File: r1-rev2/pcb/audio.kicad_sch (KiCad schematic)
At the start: 22 parts, among them J4 HP_3.5mm, J5 LO_3.5mm, Q2 AO3401A, Q3 AO3401A, U6 TLV320AIC3104

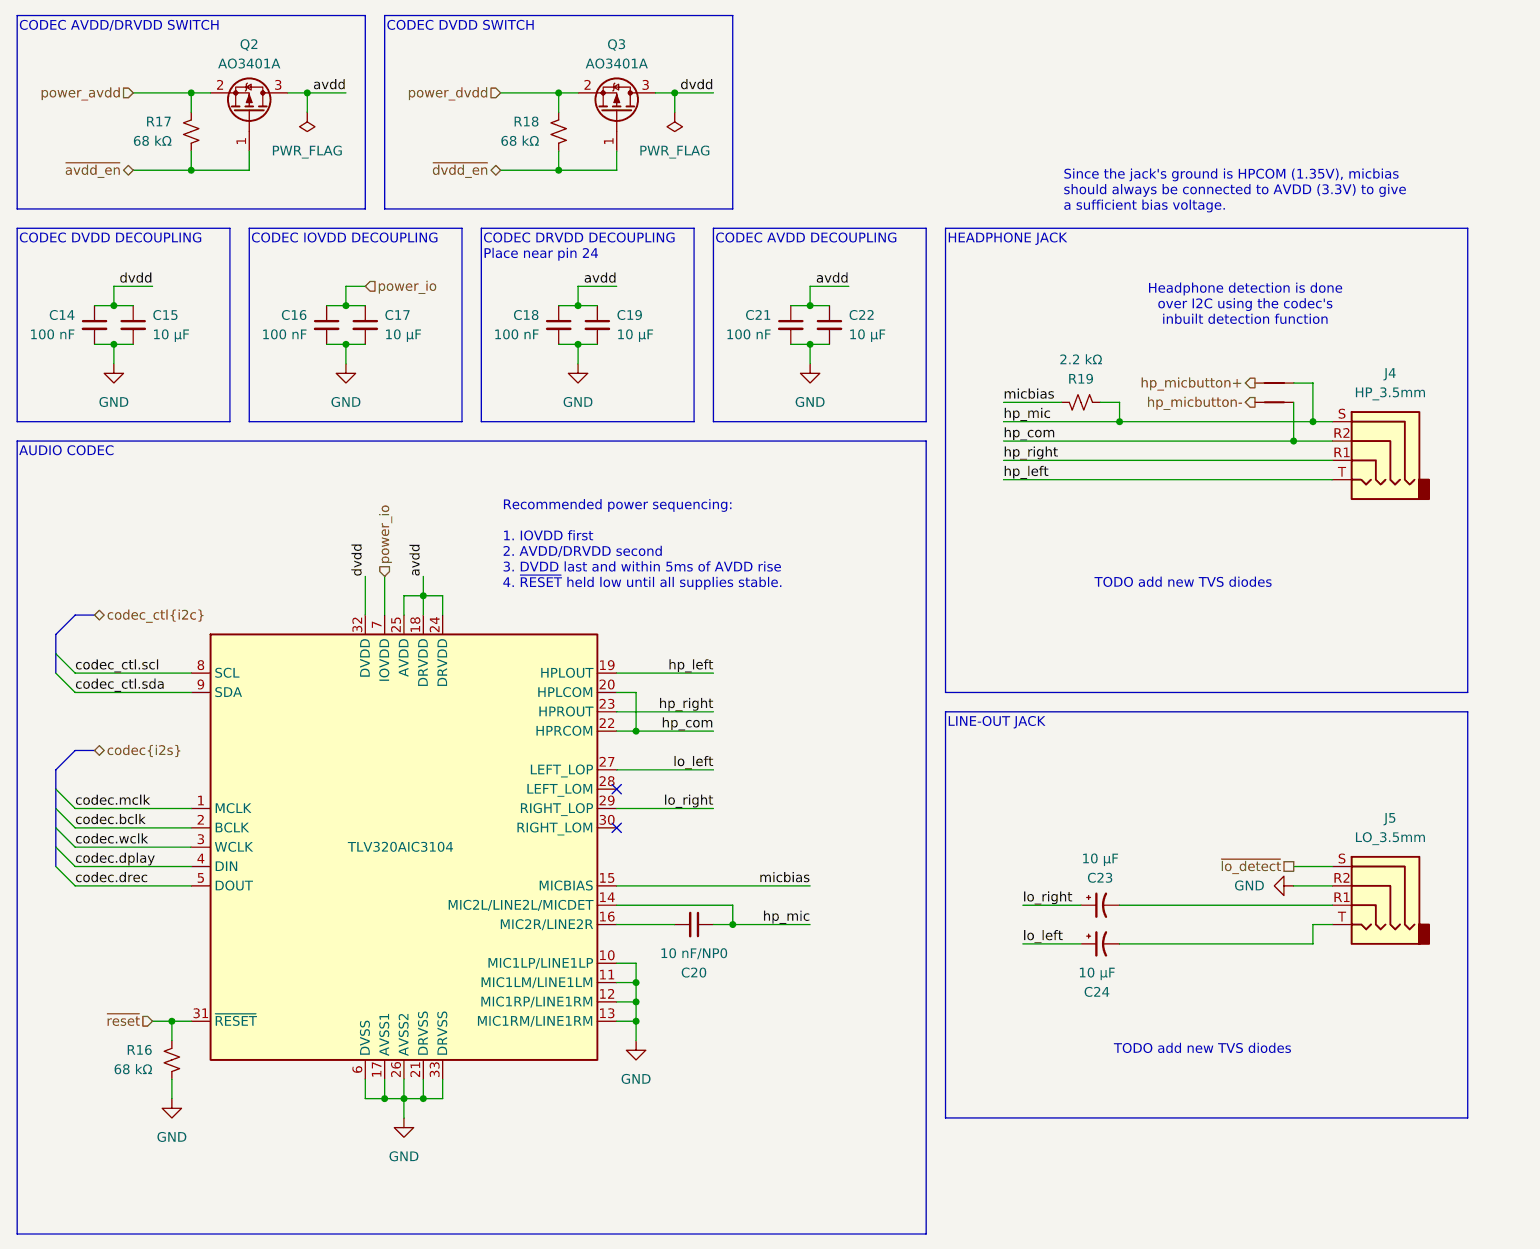
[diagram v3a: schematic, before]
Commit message: R1-Rev2: add TVS diodes to external connectors
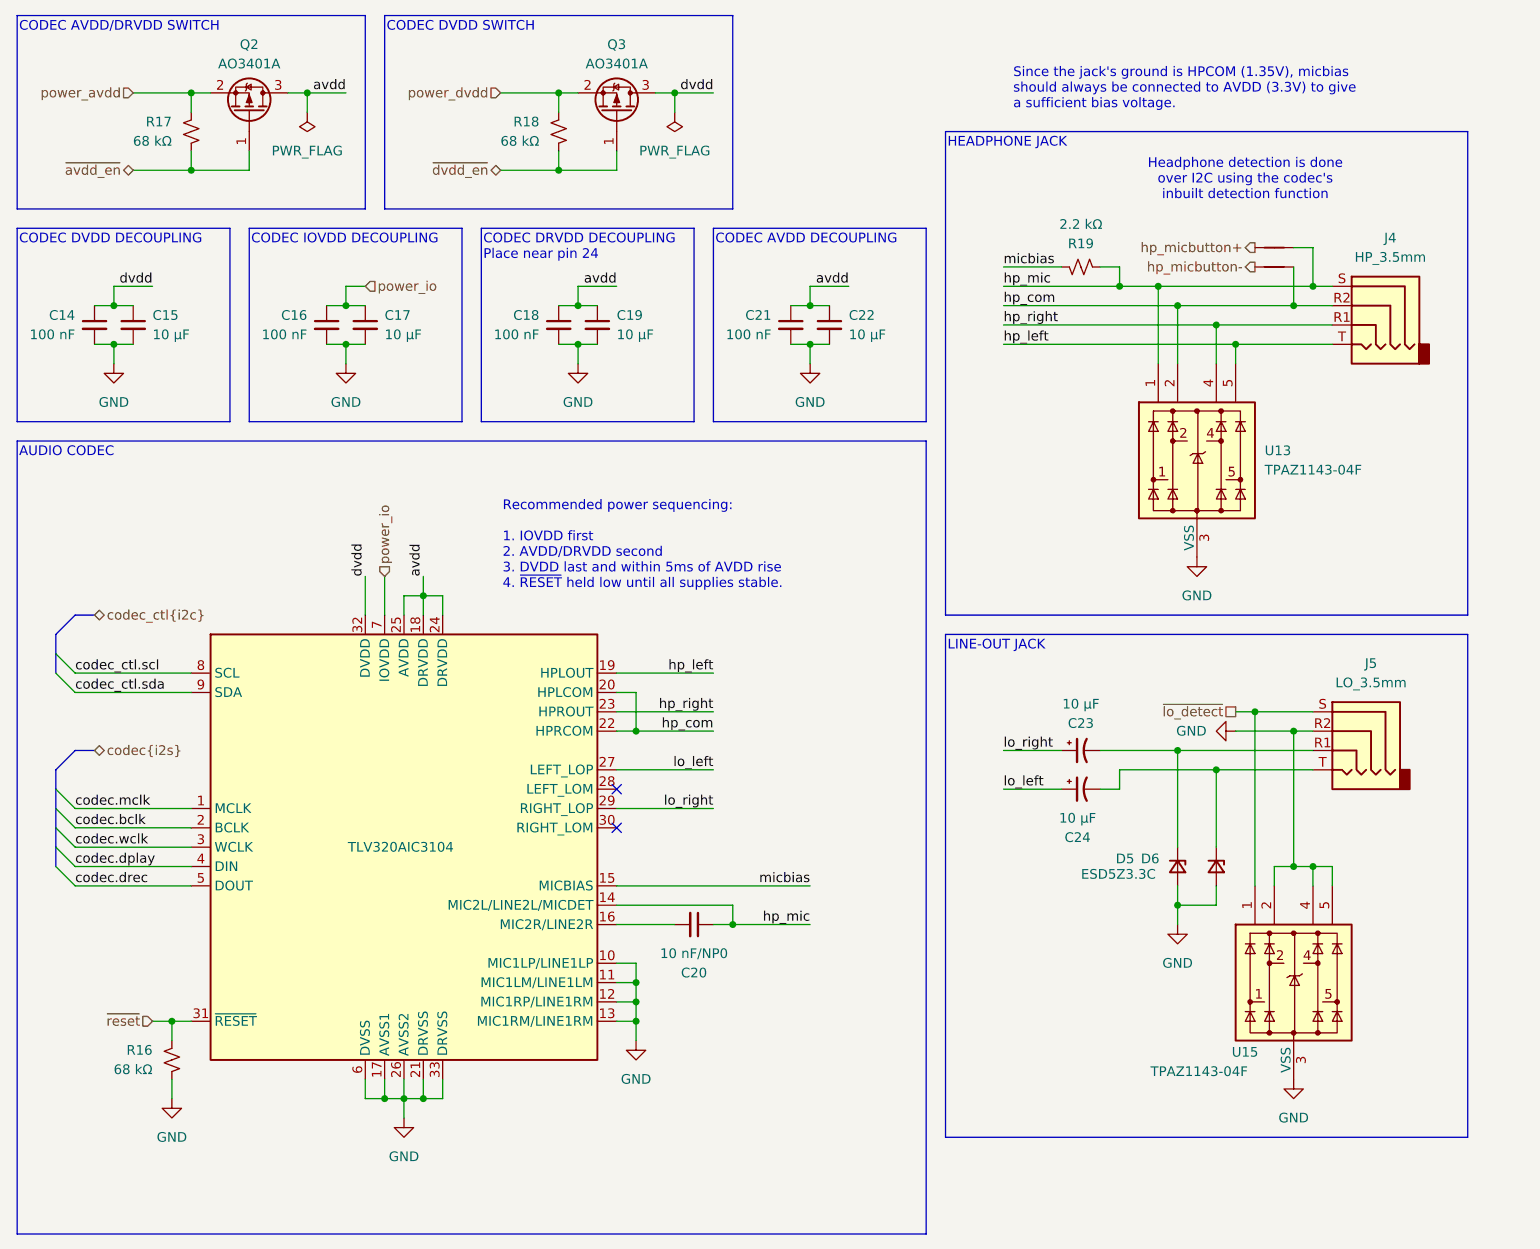
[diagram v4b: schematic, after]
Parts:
- added D5, D6: ESD5Z3.3C, Diode_SMD:D_SOD-523, symbol Device:D_Zener_Small
- added U13, U15: TPAZ1143-04F, echoplayer:TECHPUBLIC_UDFN-10_1.0x2.5mm_P0.5mm, symbol echoplayer:TPAZ1143-04F
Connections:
- net GND: now also D5.2 (A), D6.2 (A), U13.10 (NC), U13.3 (VSS), U13.6 (NC), U13.7 (NC), U13.8 (VSS), U13.9 (NC), U15.10 (NC), U15.2, U15.3 (VSS), U15.4, U15.5, U15.6 (NC), U15.7 (NC), U15.8 (VSS), U15.9 (NC)
- net hp_com: now also U13.2
- net hp_left: now also U13.5
- net hp_mic: now also U13.1
- net hp_right: now also U13.4
- net ~{lo_detect}: now also U15.1
- net at C23.2, J5.R1: now also D5.1 (K)
- net at C24.2, J5.T: now also D6.1 (K)
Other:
- note removed: "TODO add new TVS diodes"
- moved on the sheet: C23, C24, J4, J5, R19

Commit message: R1-Rev2: updates to PCB layout, add HyperRAM routing
- Reannotate schematic and assign footprints for passives
- First try at HyperRAM routing
- Fixed incorrect W958D8NBYA5I pinout
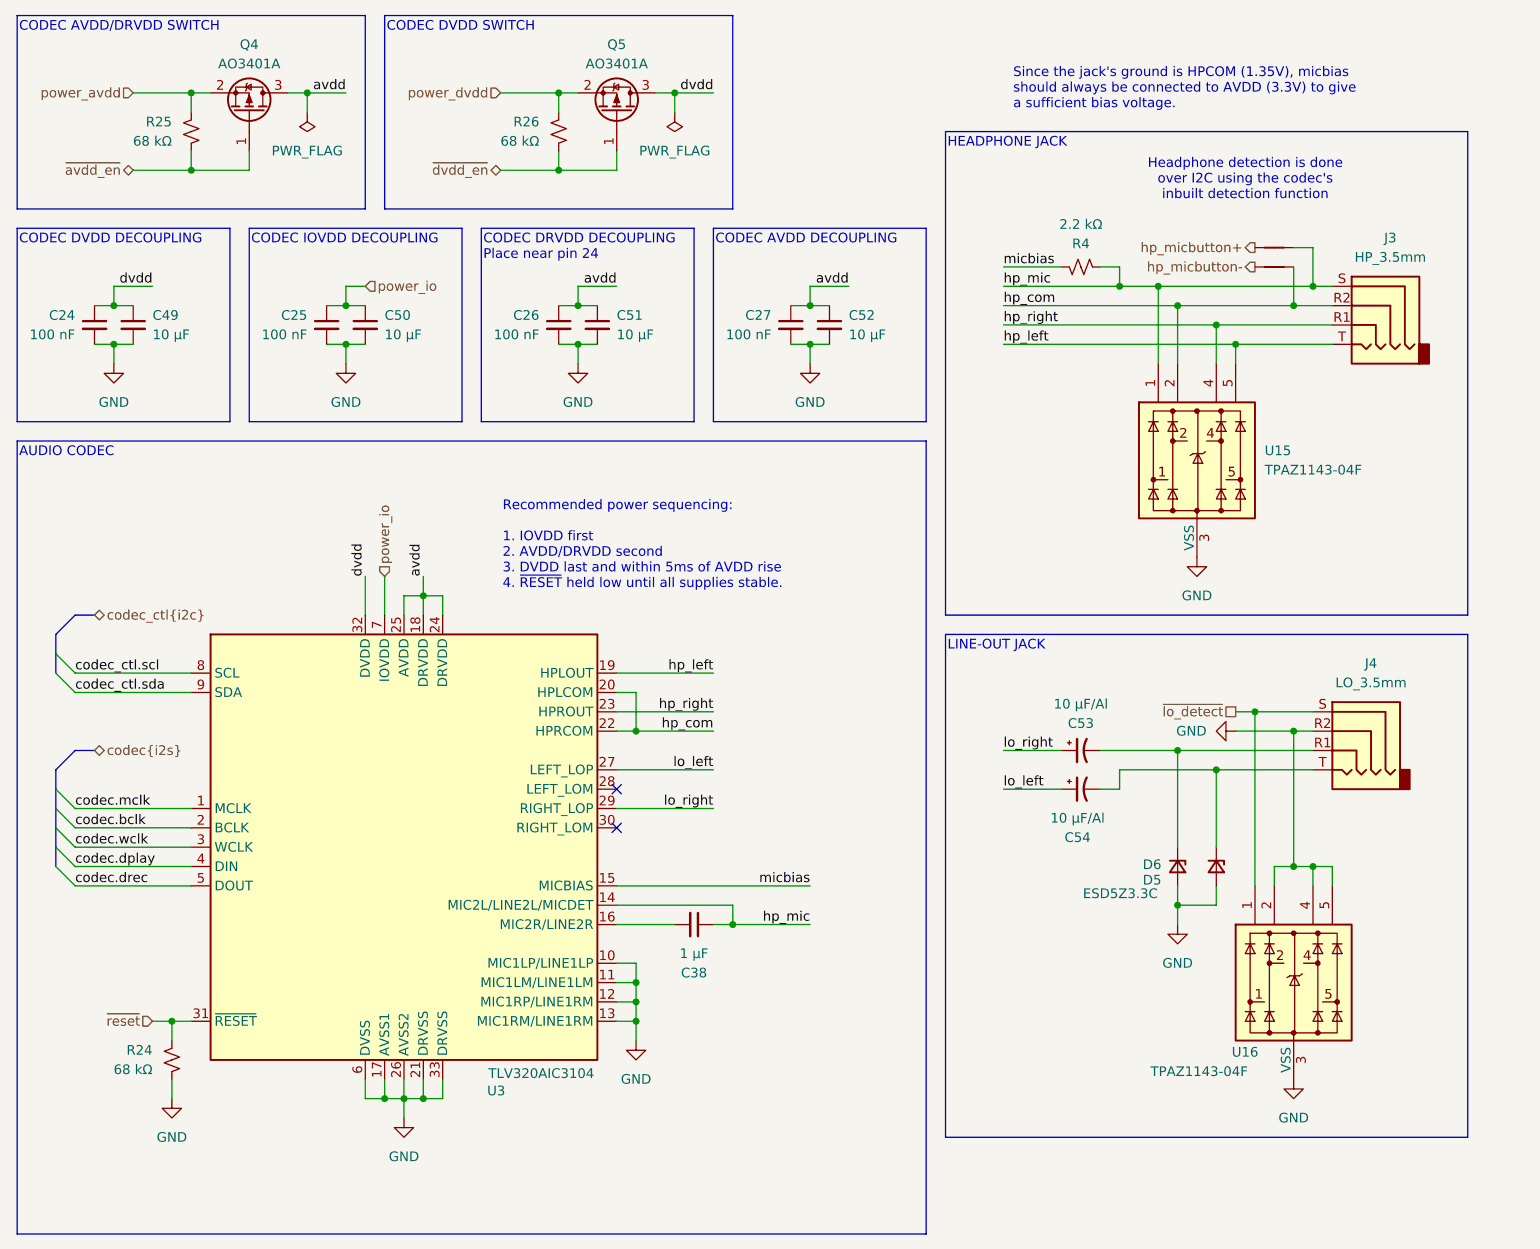
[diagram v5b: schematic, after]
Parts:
- C38: renamed from C20; value 10 nF/NP0 -> 1 µF; footprint Capacitor_SMD:C_0603_1608Metric -> Capacitor_SMD:C_0402_1005Metric
- C49: renamed from C15; footprint Capacitor_SMD:C_0603_1608Metric -> Capacitor_SMD:C_0805_2012Metric
- C50: renamed from C17; footprint Capacitor_SMD:C_0603_1608Metric -> Capacitor_SMD:C_0805_2012Metric
- C51: renamed from C19; footprint Capacitor_SMD:C_0603_1608Metric -> Capacitor_SMD:C_0805_2012Metric
- C52: renamed from C22; footprint Capacitor_SMD:C_0603_1608Metric -> Capacitor_SMD:C_0805_2012Metric
- C53: renamed from C23; value 10 µF -> 10 µF/Al
- C54: renamed from C24; value 10 µF -> 10 µF/Al
- renumbered C14 to C24, C16 to C25, C18 to C26, C21 to C27, J4 to J3, J5 to J4, NT1 to NT6, NT2 to NT7, Q2 to Q4, Q3 to Q5, R16 to R24, R17 to R25, R18 to R26, R19 to R4, U13 to U15, U15 to U16, U6 to U3

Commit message: R1-Rev2: improve reset circuit, add XSPI CS pullup
Connect NRST to xspi_reset and the regulator power-good signals.
This should ensure that the STM32 and RAM will stay in reset
until both power rails have started up. It shouldn't be necessary
to control xspi_reset with a GPIO, but for now leave it connected
just in case.

The XSPI CS pin also requires an external pullup to guarantee it
will be pulled high during power-on, which is required to ensure
the RAM resets properly.
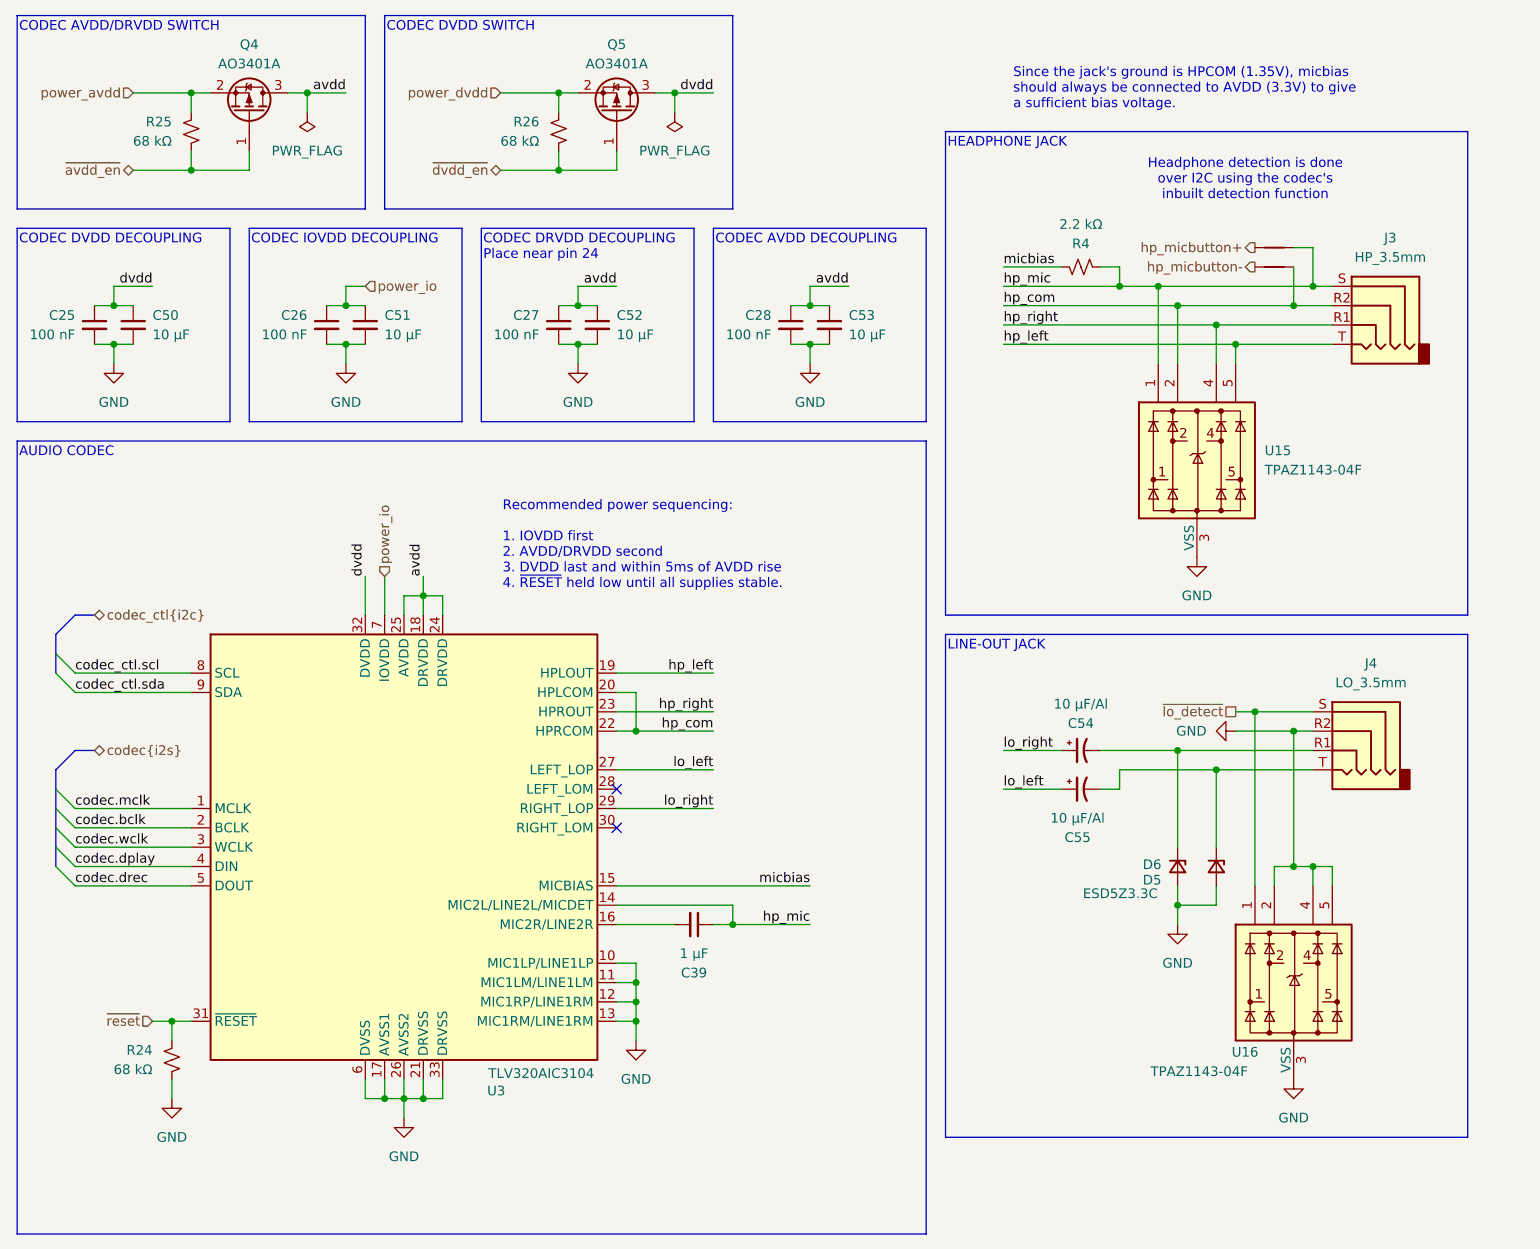
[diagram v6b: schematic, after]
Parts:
- renumbered C24 to C25, C25 to C26, C26 to C27, C27 to C28, C38 to C39, C49 to C50, C50 to C51, C51 to C52, C52 to C53, C53 to C54, C54 to C55
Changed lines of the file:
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@@
 		(on_board yes)
 		(dnp no)
-		(property "Reference" "C25"
+		(property "Reference" "C26"
 			(at 91.44 54.6162 0)
 			(effects
@@
 			(project "echo-r1"
 				(path "/aa241847-30f4-429d-a148-6a6e39ba98e0/dae5d6c8-3920-4253-a171-1dbab60b78bd"
-					(reference "C25")
+					(reference "C26")
 					(unit 1)
 				)
@@
 		(on_board yes)
 		(dnp no)
-		(property "Reference" "C51"
+		(property "Reference" "C52"
 			(at 132.08 54.6162 0)
 			(effects
@@
 			(project "echo-r1"
 				(path "/aa241847-30f4-429d-a148-6a6e39ba98e0/dae5d6c8-3920-4253-a171-1dbab60b78bd"
-					(reference "C51")
+					(reference "C52")
 					(unit 1)
 				)
@@
 		(on_board yes)
 		(dnp no)
-		(property "Reference" "C49"
+		(property "Reference" "C50"
 			(at 71.12 54.6162 0)
 			(effects
@@
 			(project "echo-r1"
 				(path "/aa241847-30f4-429d-a148-6a6e39ba98e0/dae5d6c8-3920-4253-a171-1dbab60b78bd"
-					(reference "C49")
+					(reference "C50")
 					(unit 1)
 				)
@@
 		(on_board yes)
 		(dnp no)
-		(property "Reference" "C50"
+		(property "Reference" "C51"
 			(at 101.6 54.6162 0)
 			(effects
@@
 			(project "echo-r1"
 				(path "/aa241847-30f4-429d-a148-6a6e39ba98e0/dae5d6c8-3920-4253-a171-1dbab60b78bd"
-					(reference "C50")
+					(reference "C51")
 					(unit 1)
 				)
@@
 		(on_board yes)
 		(dnp no)
-		(property "Reference" "C38"
+		(property "Reference" "C39"
 			(at 142.2336 140.97 90)
 			(effects
@@
 			(project ""
 				(path "/aa241847-30f4-429d-a148-6a6e39ba98e0/dae5d6c8-3920-4253-a171-1dbab60b78bd"
-					(reference "C38")
+					(reference "C39")
 					(unit 1)
 				)
@@
 		(on_board yes)
 		(dnp no)
-		(property "Reference" "C53"
+		(property "Reference" "C54"
 			(at 193.04 108.204 90)
 			(effects
@@
 			(project "echo-r1"
 				(path "/aa241847-30f4-429d-a148-6a6e39ba98e0/dae5d6c8-3920-4253-a171-1dbab60b78bd"
-					(reference "C53")
+					(reference "C54")
 					(unit 1)
 				)
@@
 		(on_board yes)
 		(dnp no)
-		(property "Reference" "C27"
+		(property "Reference" "C28"
 			(at 152.4 54.6162 0)
 			(effects
@@
 			(project "echo-r1"
 				(path "/aa241847-30f4-429d-a148-6a6e39ba98e0/dae5d6c8-3920-4253-a171-1dbab60b78bd"
-					(reference "C27")
+					(reference "C28")
 					(unit 1)
 				)
@@
 		(on_board yes)
 		(dnp no)
-		(property "Reference" "C24"
+		(property "Reference" "C25"
 			(at 60.96 54.6162 0)
 			(effects
@@
 			(project "echo-r1"
 				(path "/aa241847-30f4-429d-a148-6a6e39ba98e0/dae5d6c8-3920-4253-a171-1dbab60b78bd"
-					(reference "C24")
+					(reference "C25")
 					(unit 1)
 				)
@@
 		(on_board yes)
 		(dnp no)
-		(property "Reference" "C54"
+		(property "Reference" "C55"
 			(at 192.6082 123.19 90)
 			(effects
@@
 			(project "echo-r1"
 				(path "/aa241847-30f4-429d-a148-6a6e39ba98e0/dae5d6c8-3920-4253-a171-1dbab60b78bd"
-					(reference "C54")
+					(reference "C55")
 					(unit 1)
 				)
@@
 		(on_board yes)
 		(dnp no)
-		(property "Reference" "C52"
+		(property "Reference" "C53"
 			(at 162.56 54.6162 0)
 			(effects
@@
 			(project "echo-r1"
 				(path "/aa241847-30f4-429d-a148-6a6e39ba98e0/dae5d6c8-3920-4253-a171-1dbab60b78bd"
-					(reference "C52")
+					(reference "C53")
 					(unit 1)
 				)
@@
 		(on_board yes)
 		(dnp no)
-		(property "Reference" "C26"
+		(property "Reference" "C27"
 			(at 121.92 54.6162 0)
 			(effects
@@
 			(project "echo-r1"
 				(path "/aa241847-30f4-429d-a148-6a6e39ba98e0/dae5d6c8-3920-4253-a171-1dbab60b78bd"
-					(reference "C26")
-					(unit 1)
-				)
+					(reference "C27")
+					(unit 1)
+				)

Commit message: R1-Rev2: update pin assignment; add internal memory card slot
- Removed old H743 and H7R3 LQFP144 pin assignment sheets
- Updated pin assignments to make room for a 2nd card slot
- Added internal memory card slot
- Unassigned GPIOs and removed WIP routing
- Fixed net tie reference designators
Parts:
- renumbered NT6 to NT5, NT7 to NT6
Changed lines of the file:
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@@
 		(dnp no)
 		(fields_autoplaced yes)
-		(property "Reference" "NT6"
+		(property "Reference" "NT5"
 			(at 218.44 40.64 0)
 			(effects
@@
 			(project "echo-r1"
 				(path "/aa241847-30f4-429d-a148-6a6e39ba98e0/dae5d6c8-3920-4253-a171-1dbab60b78bd"
-					(reference "NT6")
+					(reference "NT5")
 					(unit 1)
 				)
@@
 		(dnp no)
 		(fields_autoplaced yes)
-		(property "Reference" "NT7"
+		(property "Reference" "NT6"
 			(at 218.44 43.18 0)
 			(effects
@@
 			(project "echo-r1"
 				(path "/aa241847-30f4-429d-a148-6a6e39ba98e0/dae5d6c8-3920-4253-a171-1dbab60b78bd"
-					(reference "NT7")
-					(unit 1)
-				)
+					(reference "NT6")
+					(unit 1)
+				)
